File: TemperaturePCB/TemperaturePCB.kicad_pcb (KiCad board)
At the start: 2 copper layers, 16 x 24.8 mm, 3 parts, among them J1 Conn_01x02_Socket

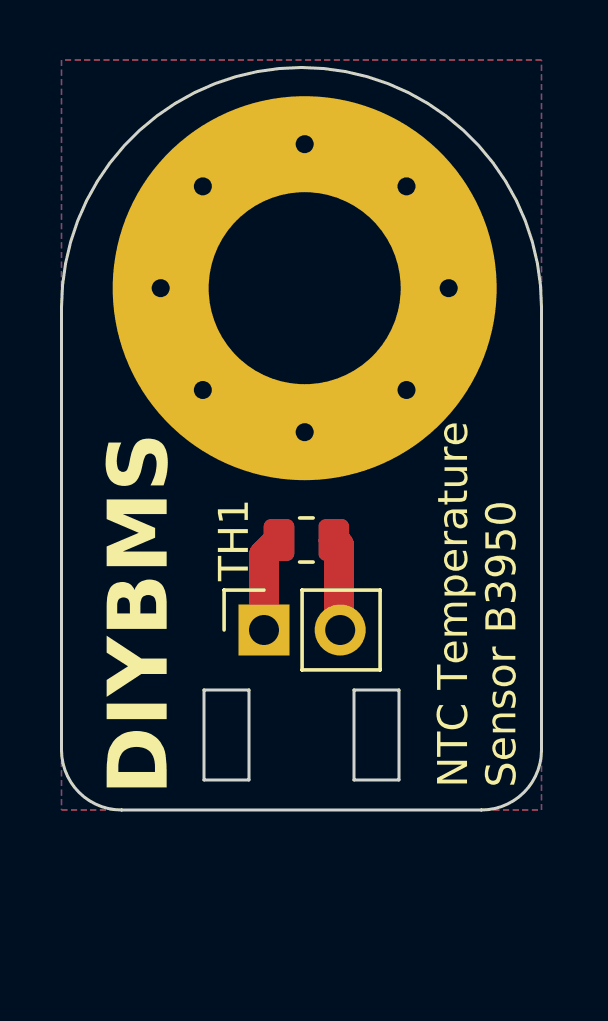
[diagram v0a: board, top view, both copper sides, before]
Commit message: Updated temperature sensor PCB board
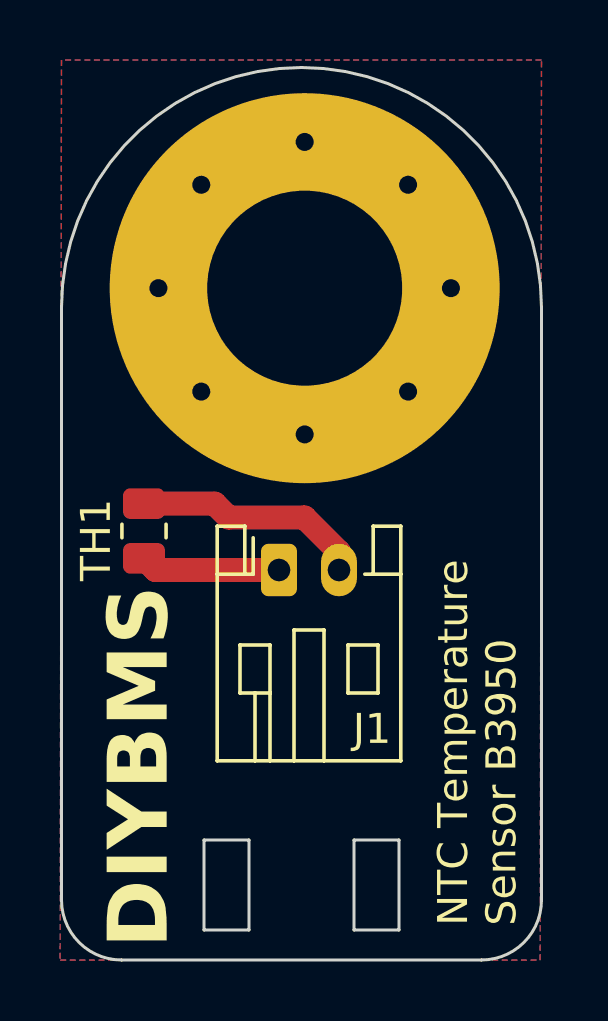
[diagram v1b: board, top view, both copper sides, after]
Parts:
- H1: footprint MountingHole:MountingHole_6.4mm_M6_Pad_Via -> MountingHole:MountingHole_6.5mm_Pad_Via
- J1: value Conn_01x02_Socket -> S2B-PH-K(LF)(SN); footprint Connector_PinSocket_2.54mm:PinSocket_1x02_P2.54mm_Vertical -> Connector_JST:JST_PH_S2B-PH-K_1x02_P2.00mm_Horizontal
- moved TH1 5.42 mm to (136.0, 104.7), turned to 90 degrees
- moved J1 2.06 mm to (140.5, 106.0), turned to 0 degrees
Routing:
- net Net-(J1-Pin_2): track 3.09 -> 7.77 mm
- net Net-(J1-Pin_1): track 3.21 -> 4.66 mm
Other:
- board size 16 x 24.8 mm -> 16 x 29.8 mm

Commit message: Swap JST_PH_S2B-PH-K_1x02 to SMD PH-SM4-TB
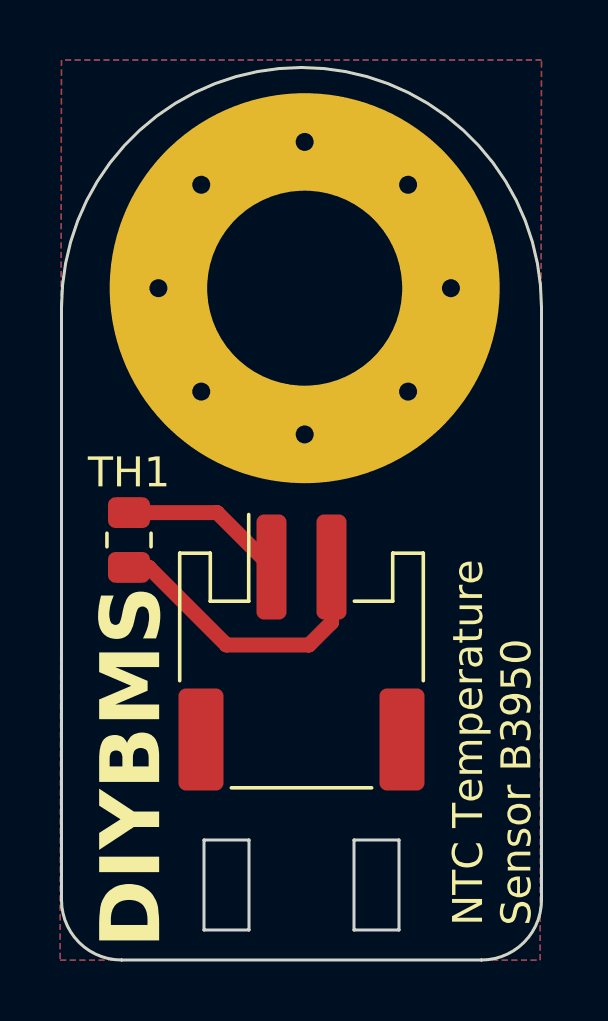
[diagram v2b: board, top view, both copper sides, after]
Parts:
- J1: value S2B-PH-K(LF)(SN) -> S2B-PH-SM4-TB(LF)(SN); footprint Connector_JST:JST_PH_S2B-PH-K_1x02_P2.00mm_Horizontal -> Connector_JST:JST_PH_S2B-PH-SM4-TB_1x02-1MP_P2.00mm_Horizontal
- moved J1 2.85 mm to (141.2, 108.8)
- moved TH1 0.58 mm to (135.5, 105.0)
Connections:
- TH1 pad 1: Net-(J1-Pin_1) -> Net-(J1-Pin_2)
- TH1 pad 2: Net-(J1-Pin_2) -> Net-(J1-Pin_1)
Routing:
- net Net-(J1-Pin_2): track 7.77 -> 9.98 mm
- net Net-(J1-Pin_1): track 4.66 -> 5.50 mm
